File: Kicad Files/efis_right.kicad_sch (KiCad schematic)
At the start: 28 parts, among them J16 L_FD, J17 L_LS, J18 L_CSTR, J19 L_WPT, J20 L_VORD, J21 L_NDB, J22 L_ARPT, J51 LB_PULL, J51 LB_PUSH, J52 LB_ENC, J53 LB_hPa/inHg, J53 LVOR/ADF_1, J54 LVOR/ADF_2, J55 L_MAP_MODE, J57 L_MAP_RANGE, U3 CD74HC4067M, U4 CD74HC4067M

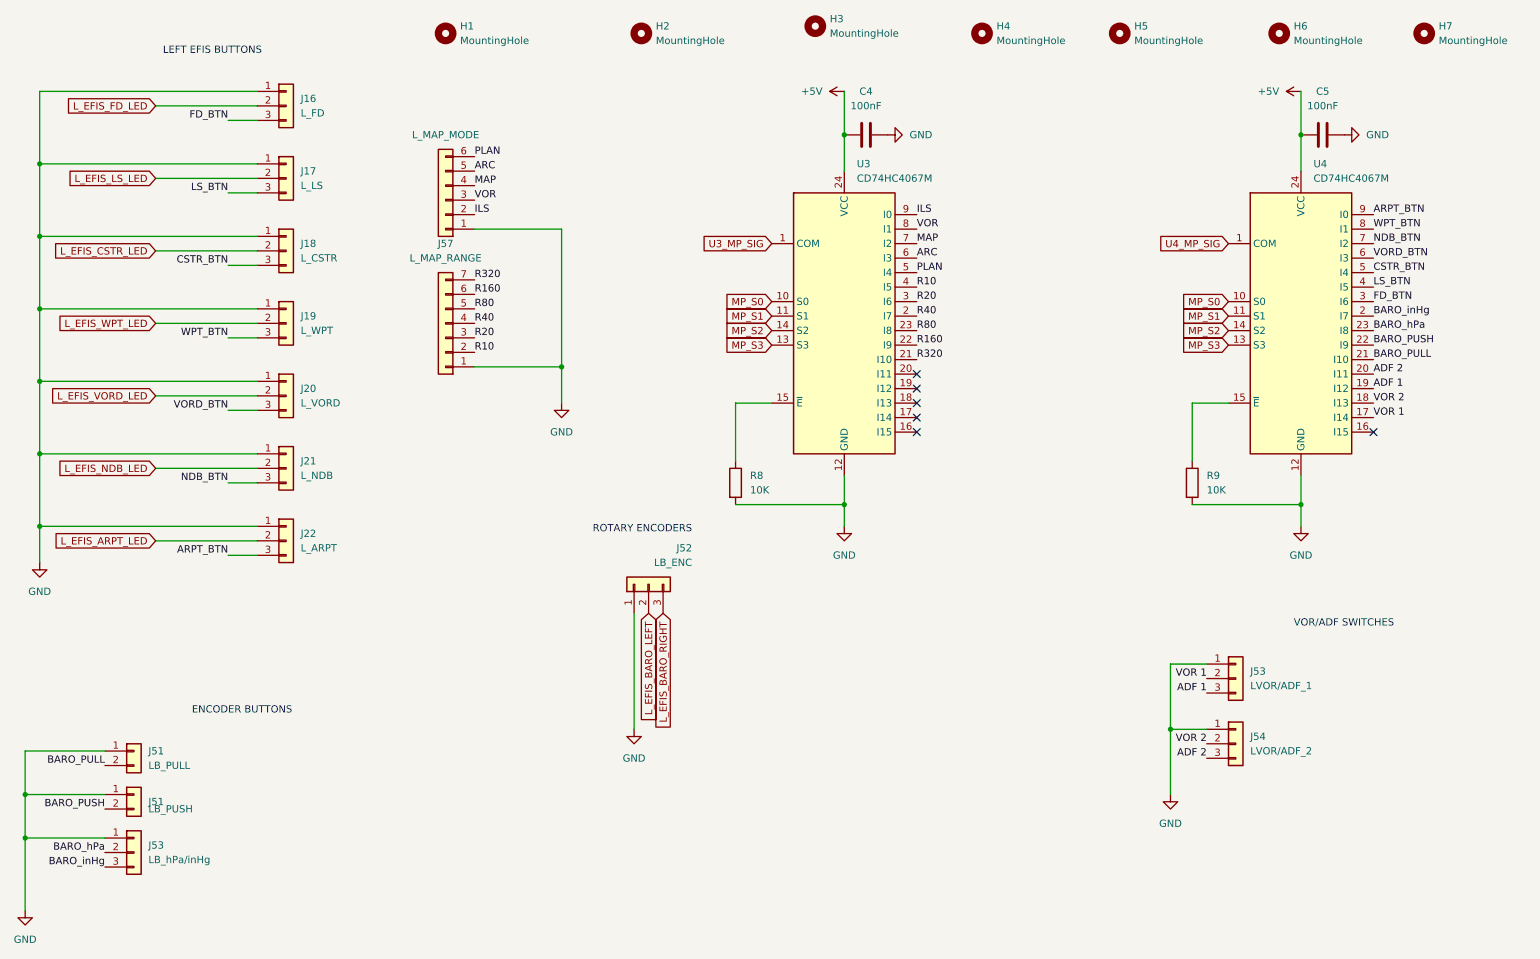
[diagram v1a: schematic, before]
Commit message: Complete rework of panels to be printed facedown. Important: change the order of the colors as Grey, White, Black, Transparent if using a Bambulab P1S/X1C ALso corrected some issue with the PCB (optional, you can print the FCU without using my pcb)
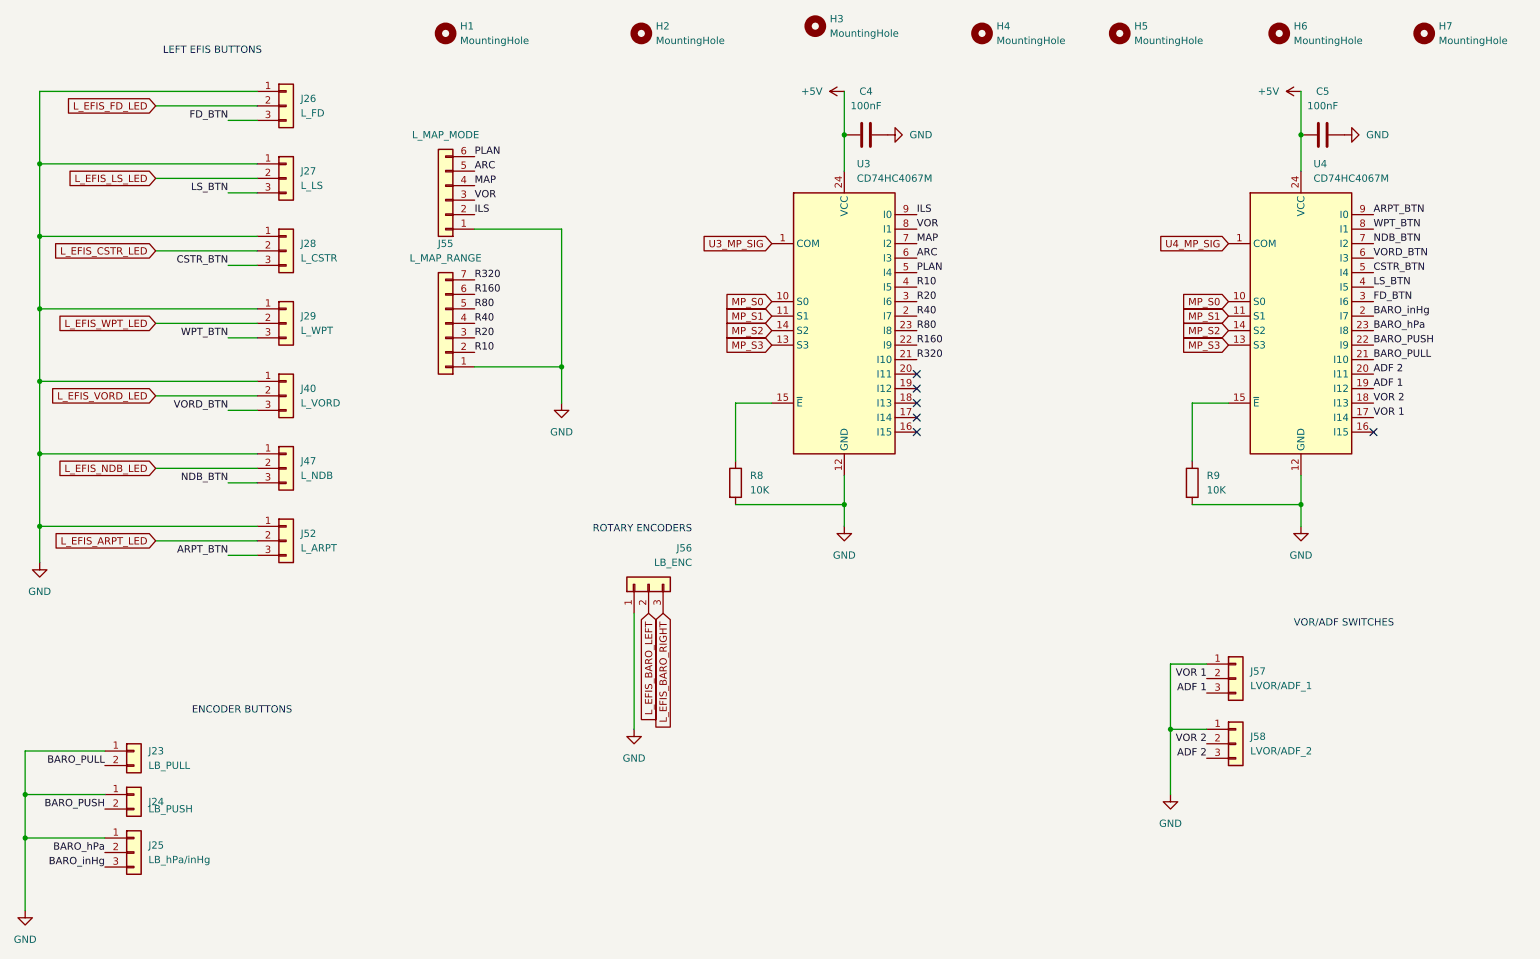
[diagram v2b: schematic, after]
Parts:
- renumbered J51 to J23, J51 to J24, J53 to J25, J16 to J26, J17 to J27, J18 to J28, J19 to J29, J20 to J40, J21 to J47, J22 to J52, J55 to J54, J57 to J55, J52 to J56, J53 to J57, J54 to J58
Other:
- title: (none) -> FCU Mainboard schematics
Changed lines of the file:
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@@
 (kicad_sch
-	(version 20231120)
+	(version 20250114)
 	(generator "eeschema")
-	(generator_version "8.0")
+	(generator_version "9.0")
 	(paper "A4")
+	(title_block
+		(title "FCU Mainboard schematics")
+		(date "2024-03-05")
+		(rev "1.0")
+	)
+	(text "LEFT EFIS BUTTONS"
+		(exclude_from_sim no)
+		(at 49.53 24.13 0)
+		(effects
+			(font
+				(size 1.27 1.27)
+			)
+			(justify left bottom)
+		)
+	)
+	(text "ROTARY ENCODERS"
+		(exclude_from_sim no)
+		(at 142.24 107.95 0)
+		(effects
+			(font
+				(size 1.27 1.27)
+			)
+			(justify right bottom)
+		)
+	)
+	(text "ENCODER BUTTONS"
+		(exclude_from_sim no)
+		(at 54.61 139.7 0)
+		(effects
+			(font
+				(size 1.27 1.27)
+			)
+			(justify left bottom)
+		)
+	)
+	(text "VOR/ADF SWITCHES"
+		(exclude_from_sim no)
+		(at 247.65 124.46 0)
+		(effects
+			(font
+				(size 1.27 1.27)
+			)
+			(justify left bottom)
+		)
+	)
 	(junction
 		(at 25.4 161.29)
@@
 		)
 	)
-	(text "LEFT EFIS BUTTONS"
-		(exclude_from_sim no)
-		(at 49.53 24.13 0)
-		(effects
-			(font
-				(size 1.27 1.27)
-			)
-			(justify left bottom)
-		)
-	)
-	(text "ROTARY ENCODERS"
-		(exclude_from_sim no)
-		(at 142.24 107.95 0)
-		(effects
-			(font
-				(size 1.27 1.27)
-			)
-			(justify right bottom)
-		)
-	)
-	(text "ENCODER BUTTONS"
-		(exclude_from_sim no)
-		(at 54.61 139.7 0)
-		(effects
-			(font
-				(size 1.27 1.27)
-			)
-			(justify left bottom)
-		)
-	)
-	(text "VOR/ADF SWITCHES"
-		(exclude_from_sim no)
-		(at 247.65 124.46 0)
-		(effects
-			(font
-				(size 1.27 1.27)
-			)
-			(justify left bottom)
-		)
-	)
 	(label "R40"
 		(at 181.61 69.85 0)
@@
 		(dnp no)
 		(fields_autoplaced yes)
-		(property "Reference" "J16"
+		(property "Reference" "J26"
 			(at 73.66 31.7499 0)
 			(effects
@@
 		(dnp no)
 		(fields_autoplaced yes)
-		(property "Reference" "J18"
+		(property "Reference" "J28"
 			(at 73.66 57.1499 0)
 			(effects
@@
 		(dnp no)
 		(fields_autoplaced yes)
-		(property "Reference" "J55"
+		(property "Reference" "J54"
 			(at 92.71 48.26 90)
 			(effects
@@
 		(dnp no)
 		(fields_autoplaced yes)
-		(property "Reference" "J20"
+		(property "Reference" "J40"
 			(at 73.66 82.5499 0)
 			(effects
@@
 		(dnp no)
 		(fields_autoplaced yes)
-		(property "Reference" "J19"
+		(property "Reference" "J29"
 			(at 73.66 69.8499 0)
 			(effects
@@
 		(dnp no)
 		(fields_autoplaced yes)
-		(property "Reference" "J22"
+		(property "Reference" "J52"
 			(at 73.66 107.9499 0)
 			(effects
@@
 		(dnp no)
 		(fields_autoplaced yes)
-		(property "Reference" "J17"
+		(property "Reference" "J27"
 			(at 73.66 44.4499 0)
 			(effects
@@
 		(dnp no)
 		(fields_autoplaced yes)
-		(property "Reference" "J51"
+		(property "Reference" "J24"
 			(at 46.99 154.9399 0)
 			(effects
@@
 		(on_board yes)
 		(dnp no)
-		(property "Reference" "J52"
+		(property "Reference" "J56"
 			(at 142.24 110.49 90)
 			(effects
@@
 		(dnp no)
 		(fields_autoplaced yes)
-		(property "Reference" "J53"
+		(property "Reference" "J57"
 			(at 240.03 132.0799 0)
 			(effects
@@
 		(dnp no)
 		(fields_autoplaced yes)
-		(property "Reference" "J57"
+		(property "Reference" "J55"
 			(at 99.06 57.15 0)
 			(effects
@@
 		(dnp no)
 		(fields_autoplaced yes)
-		(property "Reference" "J54"
+		(property "Reference" "J58"
 			(at 240.03 143.5099 0)
 			(effects
@@
 		(dnp no)
 		(fields_autoplaced yes)
-		(property "Reference" "J51"
+		(property "Reference" "J23"
 			(at 46.99 146.0499 0)
 			(effects
@@
 		(dnp no)
 		(fields_autoplaced yes)
-		(property "Reference" "J53"
+		(property "Reference" "J25"
 			(at 46.99 162.5599 0)
 			(effects
@@
 		(dnp no)
 		(fields_autoplaced yes)
-		(property "Reference" "J21"
+		(property "Reference" "J47"
 			(at 73.66 95.2499 0)
 			(effects
